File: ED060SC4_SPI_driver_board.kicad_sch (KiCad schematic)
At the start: 10 parts, among them J1 ED060SC4, U1 TPS65185

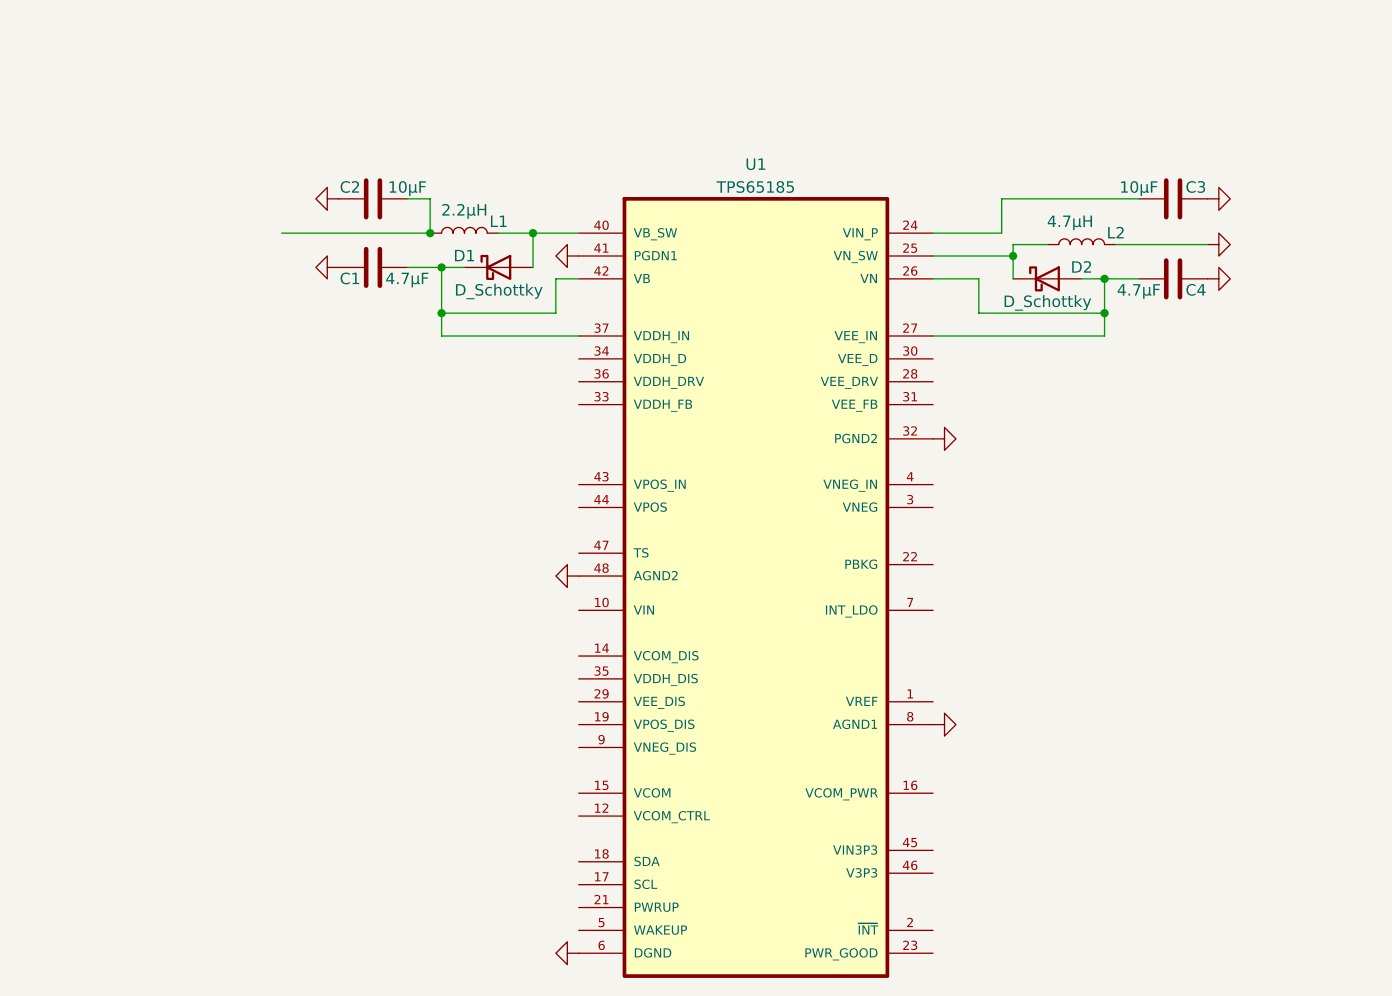
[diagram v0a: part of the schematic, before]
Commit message: Wired TPS65185 according to datasheet
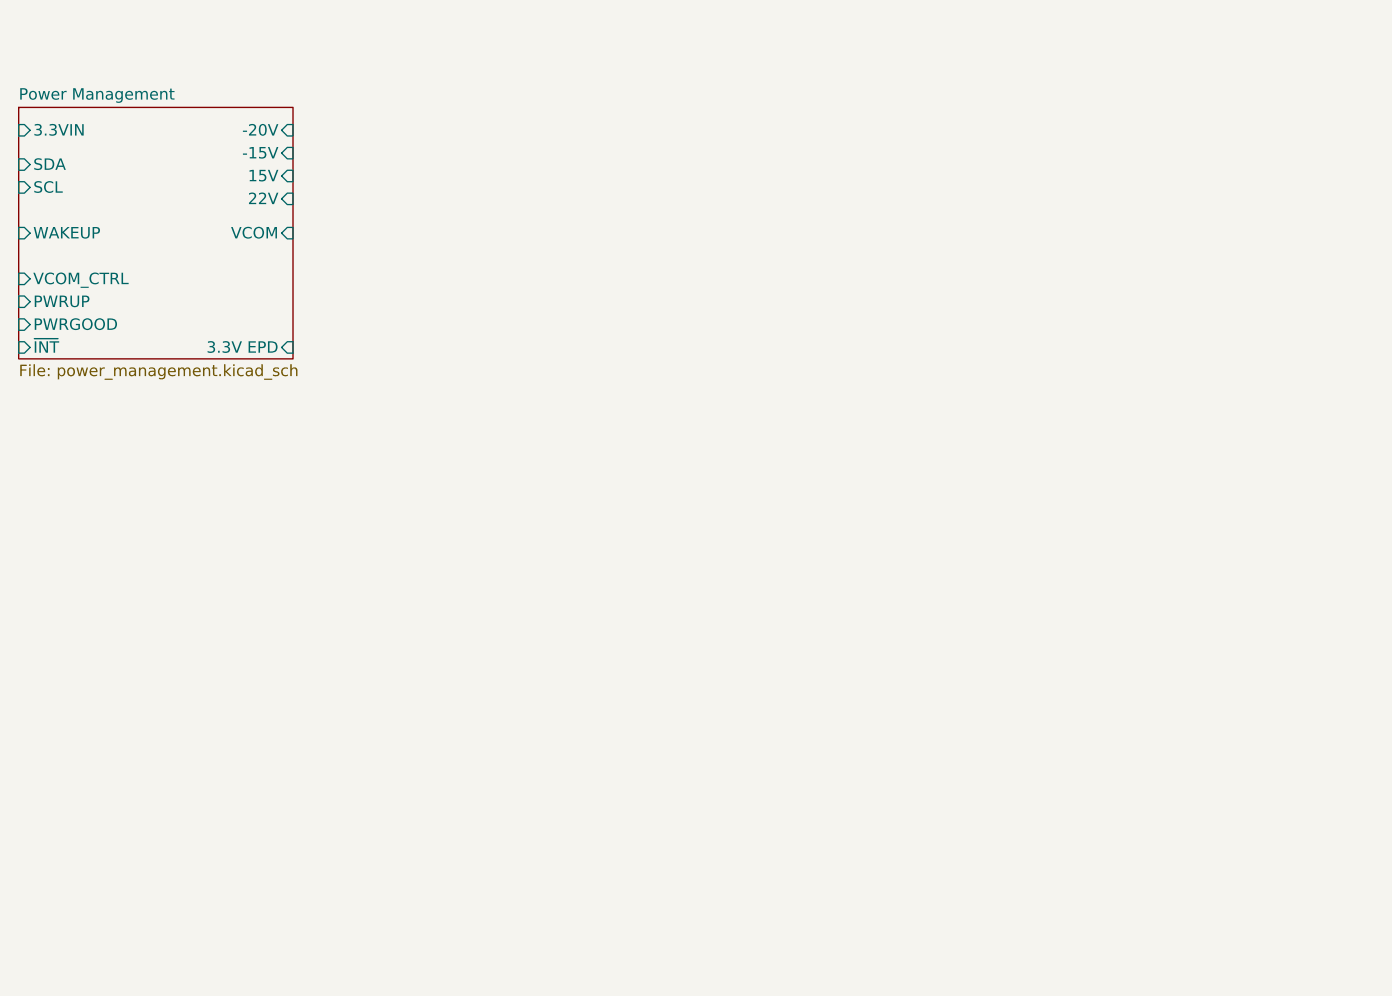
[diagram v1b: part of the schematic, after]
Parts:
- removed C1, C4: 4.7µF, symbol Device:C
- removed C2, C3: 10µF, symbol Device:C
- removed D1, D2: D_Schottky, symbol Device:D_Schottky
- removed L1: 2.2µH, symbol Device:L
- removed L2: 4.7µH, symbol Device:L
- removed U1: TPS65185, QFN50P700X700X100-49N, symbol TPS65185:TPS65185RGZR
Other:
- added sheet Power Management (power_management.kicad_sch)

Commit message: Full Schematic
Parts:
- removed J1: ED060SC4, symbol ED060SC4:ED060SC4
- added C20, C21, C22, C23, C25, C28: 100nF, symbol Device:C
- added C24: 10µF, symbol Device:C
- added C26, C27: 1µF, symbol Device:C
- added C29, C30: 10pF, symbol Device:C
- added D7: RED, symbol Device:LED
- added FB1: 120Ω@100MHz, symbol Device:FerriteBead
- added J2: Conn_01x06, symbol Connector_Generic:Conn_01x06
- added J3, J4: Conn_01x04, symbol Connector_Generic:Conn_01x04
- added R10, R12, R14: 10k, symbol Device:R
- added R11: 1k, symbol Device:R
- added SW1: SW_SPDT, symbol Switch:SW_SPDT
- added U2: STM32F103C8T6, Package_QFP:LQFP-48_7x7mm_P0.5mm, symbol MCU_ST_STM32F1:STM32F103C8Tx
- added Y1: 16MHz, 10pF, symbol Device:Crystal_GND24
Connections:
- new net +3.3V: C20.1, C21.1, C22.1, C23.1, C24.1, C27.1, D7.2 (A), FB1.2, J2.6 (Pin_6), J3.4 (Pin_4), J4.4 (Pin_4), R12.1, R14.1, SW1.3 (C), U2.1 (VBAT), U2.24 (VDD), U2.36 (VDD), U2.48 (VDD)
- new net +3.3VA: C25.1, C26.1, FB1.1, U2.9 (VDDA)
- new net BOOT0: R10.2, U2.44 (BOOT0)
- new net D0: U2.3 (PC14)
- new net D1: U2.4 (PC15)
- new net D2: U2.18 (PB0)
- new net D3: U2.19 (PB1)
- new net D4: U2.20 (PB2)
- new net D5: U2.39 (PB3)
- new net D6: U2.40 (PB4)
- new net D7: U2.41 (PB5)
- new net EPD_CKV: U2.21 (PB10)
- new net EPD_CLK: U2.10 (PA0)
- new net EPD_GMODE: U2.45 (PB8)
- new net EPD_LE: U2.12 (PA2)
- new net EPD_OE: U2.2 (PC13)
- new net EPD_SPH: U2.11 (PA1)
- new net EPD_SPV: U2.46 (PB9)
- new net GND: C20.2, C21.2, C22.2, C23.2, C24.2, C25.2, C26.2, C27.2, C28.1, C29.1, C30.1, J2.1 (Pin_1), J3.1 (Pin_1), J4.1 (Pin_1), R11.2, SW1.1 (A), U2.23 (VSS), U2.35 (VSS), U2.47 (VSS), U2.8 (VSSA), Y1.2, Y1.4
- new net HSE_IN: C29.2, U2.5 (PD0), Y1.1
- new net HSE_OUT: C30.2, U2.6 (PD1), Y1.3
- new net I2C1_SCL: R12.2, U2.42 (PB6)
- new net I2C1_SDA: R14.2, U2.43 (PB7)
- new net NRST: C28.2, U2.7 (NRST)
- new net PWR_ON_LED: D7.1 (K), R11.1
- new net SPI1_MISO: J2.3 (Pin_3), U2.16 (PA6)
- new net SPI1_MOSI: J2.2 (Pin_2), U2.17 (PA7)
- new net SPI1_SCK: J2.4 (Pin_4), U2.15 (PA5)
- new net SWCLK: J4.2 (Pin_2), U2.37 (PA14)
- new net SWDIO: J4.3 (Pin_3), U2.34 (PA13)
- new net SW_BOOT0: R10.1, SW1.2 (B)
- new net TPS_PWRGOOD: U2.27 (PB14)
- new net TPS_PWRUP: U2.25 (PB12)
- new net TPS_VCOM_CTRL: U2.26 (PB13)
- new net TPS_WAKEUP: U2.22 (PB11)
- new net TPS_~{INT}: U2.28 (PB15)
- new net USART1_RX: J3.3 (Pin_3), U2.30 (PA9)
- new net USART1_TX: J3.2 (Pin_2), U2.31 (PA10)
- new net ~{SPI1_CS}: J2.5 (Pin_5), U2.14 (PA4)
- no-connect marks 0 -> 5
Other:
- sheet Power Management renamed EPD Power Rails
- added sheet EPD ED060SC4 (epd_ed060sc4.kicad_sch)
- note added: "C = 2 * (C_{crystal} - C_{stray}) = 2 * (10pF - 5pF) = 10pF"
- note added: "EPD Screen"
- note added: "Main Power & SPI"
- note added: "Number of pins required from the µC: 32 TPS 65185: 7 (4 min) - SDA & SCL (I²C) - WAKEUP & PWRUP - PWRGOOD (Can be iomitted) - VCOM_CTRL (Can be omitted and connected to 3.3V) - ~{INT} (Can be omitted and left floating) ED060SC4: 15 - GMODE - SPV - CKV - CL - LE - OE - SPH - D0 to D7 (Data Bus) STM32F103C8 Reserved: 10 - SWD (SWCLK, SWDIO) - USART (RX, TX) - SPI (SCK, MOSI, MISO, CS) - Oscillator 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"
- note added: "Pin-out via STM32CubeMX. The I2C 10k resistor come from the TPS65185 datasheet. 100nF capacitor used on NRST to prevent from spurious resets."
- note added: "Place each 100nF close to its VDD pin"
- note added: "Power Rails"
- note added: "STM32 Microcontroller"
- note added: "Serial Wire Debug"
- note added: "This is the interface of the driver board. The user is expected to supply 3.3V and GND via this header. The commands can then be send via SPI to the MCU."
- note added: "UART - Programming"
- company: (none) -> hatrix
- title: (none) -> ED060SC4 SPI Driver Board
